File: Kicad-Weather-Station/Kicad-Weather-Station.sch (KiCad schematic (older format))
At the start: 41 parts

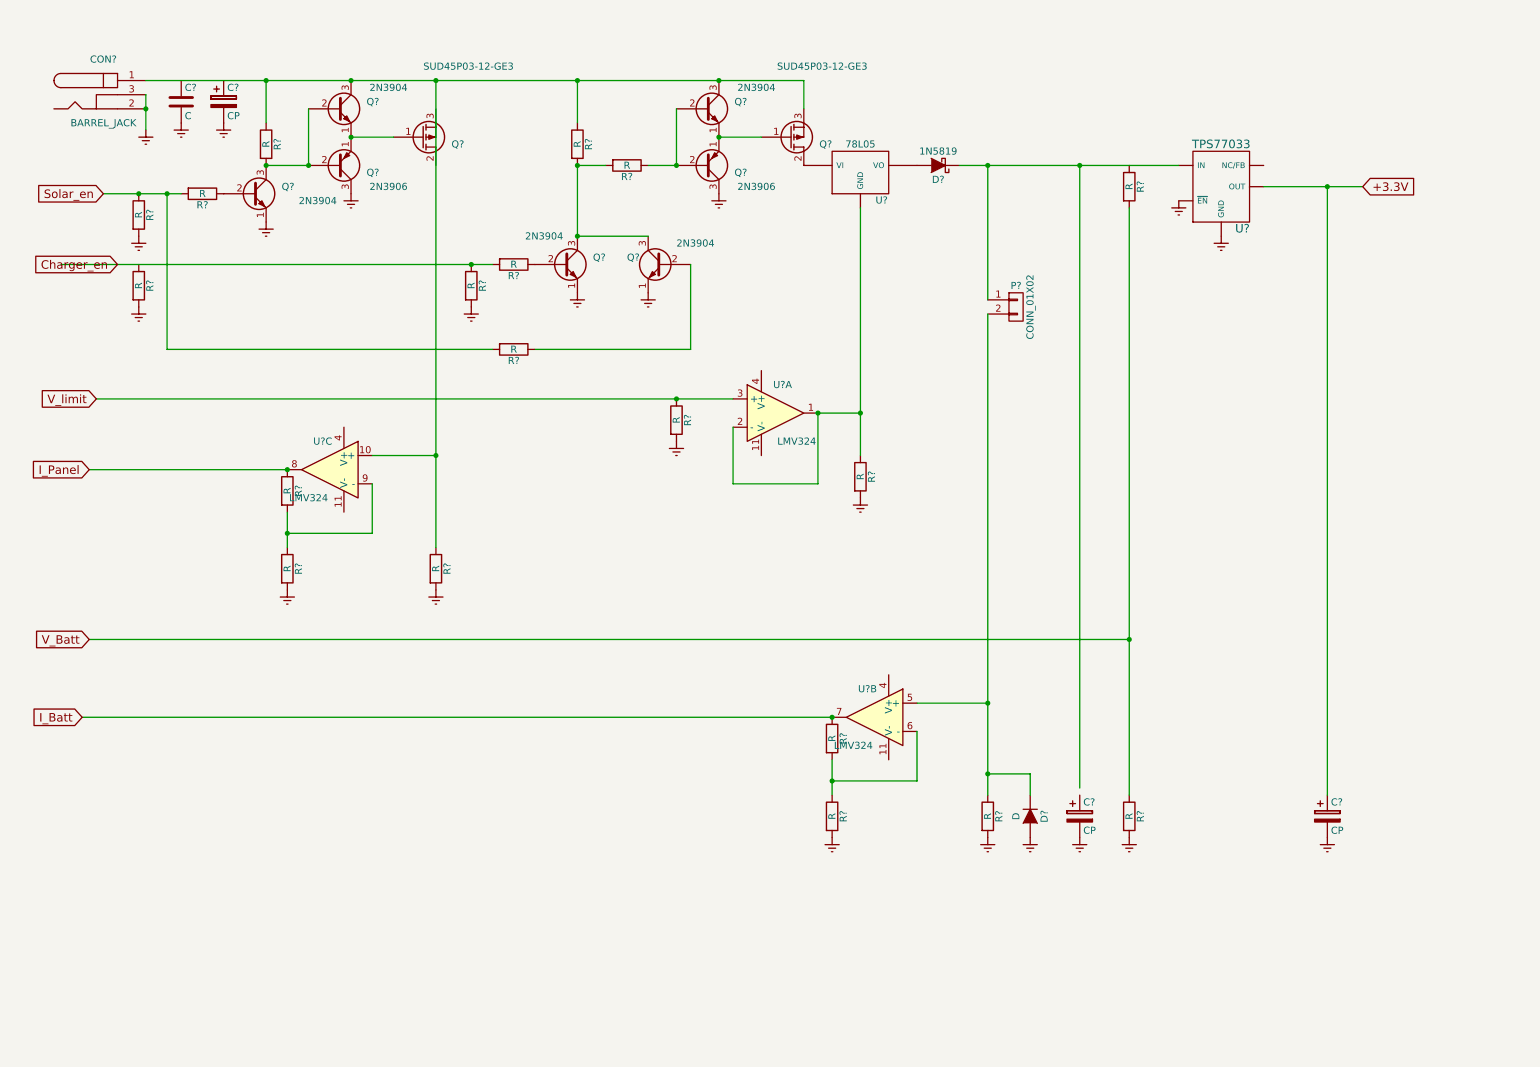
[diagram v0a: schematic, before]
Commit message: Update to schematics. Kicad version completed with values and annotation.
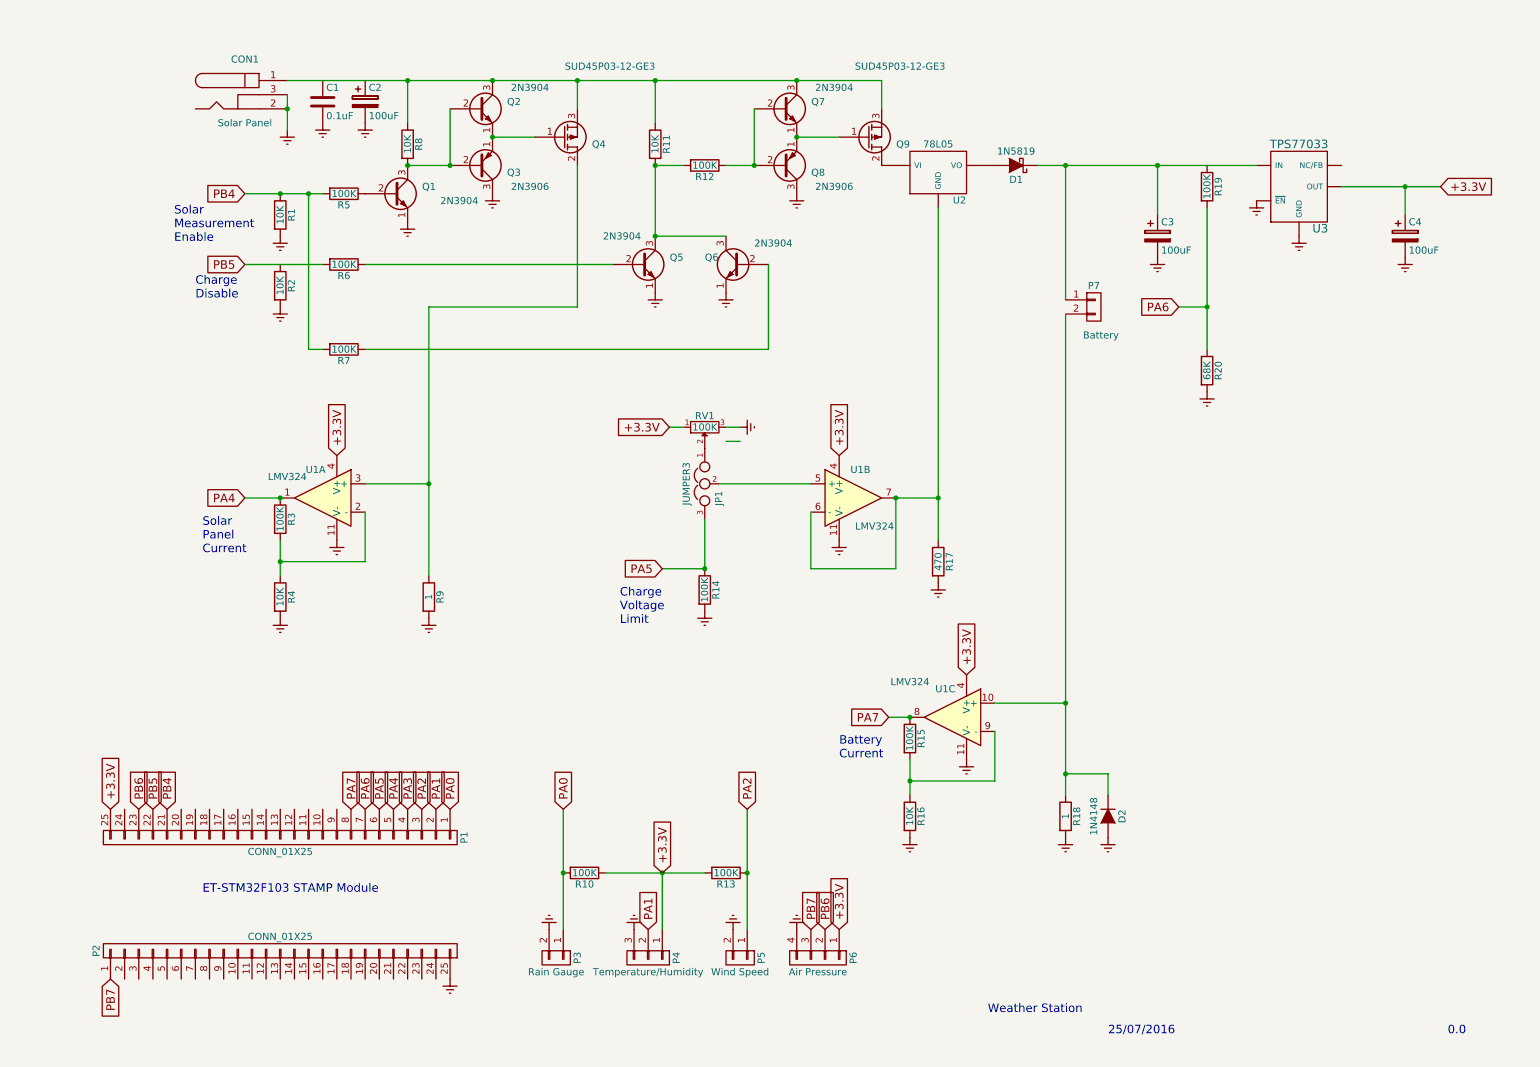
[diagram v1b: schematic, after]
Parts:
- removed R?: R, symbol R
- added JP1: JUMPER3, symbol JUMPER3
- added P1, P2: CONN_01X25, symbol CONN_01X25
- added P3: Rain Gauge, symbol CONN_01X02
- added P4: Temperature/Humidity, symbol CONN_01X03
- added P5: Wind Speed, symbol CONN_01X02
- added P6: Air Pressure, symbol CONN_01X04
- added R10, R13: 100K, symbol R
- added RV1: 100K, symbol POT
- C1: renamed from C?; value C -> 0.1uF
- C2, C3, C4: renamed from C?; value CP -> 100uF
- CON1: renamed from CON?; value BARREL_JACK -> Solar Panel
- D2: renamed from D?; value D -> 1N4148
- P7: renamed from P?; value CONN_01X02 -> Battery
- R1, R11, R16, R2, R4, R8: renamed from R?; value R -> 10K
- R12, R14, R15, R19, R3, R5, R6, R7: renamed from R?; value R -> 100K
- R17: renamed from R?; value R -> 470
- R18, R9: renamed from R?; value R -> 1
- R20: renamed from R?; value R -> 68K
- gave numbers to parts that had none: 13
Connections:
- net labels added: PA0, PA1, PA2, PA3, PA4, PA5, PA6, PA7, PB4, PB5, PB6, PB7
- net labels removed: Charger_en, I_Batt, I_Panel, Solar_en, V_Batt, V_limit
- wire segments 47 -> 81
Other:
- note added: "0.0"
- note added: "25/07/2016"
- note added: "Battery\nCurrent"
- note added: "Charge\nDisable"
- note added: "Charge\nVoltage\nLimit"
- note added: "ET-STM32F103 STAMP Module"
- note added: "Solar\nMeasurement\nEnable"
- note added: "Solar\nPanel\nCurrent"
- note added: "Weather Station"
- moved on the sheet: C1, C2, C3, C4, CON1, D1, D2, P7, Q1, Q2, Q3, Q4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

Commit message: Add footprints and create PCB. Some layout started. Trimpot footprint to be defined.
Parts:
- C1: footprint (none) -> WeatherStation:SM0603_Capa
- C2, C3, C4: footprint (none) -> WeatherStation:SM1206POL
- CON1: footprint (none) -> WeatherStation:BARREL_JACK
- D1: value 1N5819 -> MBR0520LT1G; footprint (none) -> WeatherStation:SOD-123
- D2: footprint (none) -> WeatherStation:SOD-523
- JP1, P4: footprint (none) -> WeatherStation:PINHEAD1-3
- P1, P2: footprint (none) -> WeatherStation:Pin_Header_Straight_1x25
- P3, P5, P7: footprint (none) -> WeatherStation:PINHEAD1-2
- P6: footprint (none) -> WeatherStation:PINHEAD1-4
- Q1, Q2, Q5, Q6, Q7: value 2N3904 -> MMBT3904; footprint (none) -> WeatherStation:SOT23EBC
- Q3, Q8: value 2N3906 -> MMBT3906; footprint (none) -> WeatherStation:SOT23EBC
- Q4, Q9: footprint (none) -> WeatherStation:TO-252-2Lead
- R1, R10, R11, R12, R13, R14, R15, R16, R17, R18, R19, R2, R20, R3, R4, R5, R6, R7, R8, R9: footprint (none) -> WeatherStation:SM0603_Resistor
- RV1: footprint (none) -> Potentiometers:Potentiometer_Bourns_3339P_Angular_ScrewUp
- U1: footprint (none) -> WeatherStation:SOIC-14_N
- U2: value 78L05 -> 78M05; footprint (none) -> WeatherStation:TO-252-2Lead
- U3: footprint (none) -> WeatherStation:SOT23-5
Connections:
- net labels removed: PA3
- wire segments 81 -> 60
- no-connect marks 0 -> 38

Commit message: Oops! forgot the microSD card. Rearrangement of PCB layout to accommodate.
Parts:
- removed U2: 78M05, WeatherStation:TO-252-2Lead, symbol 78L05
- added J1: MicroSD, WeatherStation:Conn_uSDcard, symbol MicroSD
- added R10, R11, R12, R13, R14: 100K, WeatherStation:SM0603_Resistor, symbol R
- added U2: 78M05, WeatherStation:TO-252-2Lead, symbol 78M05
- C4: value 100uF -> 10uF
- renumbered R10 to R15, R11 to R16, R12 to R17, R14 to R18, R13 to R19, R15 to R20, R16 to R21, R17 to R22, R18 to R23, R19 to R24, R20 to R25
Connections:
- net labels added: PB12, PB13, PB14, PB15, RSRVD
- wire segments 60 -> 61
- no-connect marks 38 -> 35
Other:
- moved on the sheet: P1, P2

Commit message: First form of PCB
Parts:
- added P10, P11, P12, P8, P9: CONN_01X01, WeatherStation:SIL-1, symbol CONN_01X01
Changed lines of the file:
@@
 Connection ~ 3850 7300
 NoConn ~ 1350 7000
+$Comp
+L CONN_01X01 P8
+U 1 1 5798030E
+P 8950 3800
+F 0 "P8" H 8950 3900 50  0000 C CNN
+F 1 "CONN_01X01" V 9050 3800 50  0000 C CNN
+F 2 "WeatherStation:SIL-1" H 8950 3800 50  0001 C CNN
+F 3 "" H 8950 3800 50  0000 C CNN
+	1    8950 3800
+	1    0    0    -1
+$EndComp
+$Comp
+L CONN_01X01 P9
+U 1 1 579803AD
+P 8950 4050
+F 0 "P9" H 8950 4150 50  0000 C CNN
+F 1 "CONN_01X01" V 9050 4050 50  0000 C CNN
+F 2 "WeatherStation:SIL-1" H 8950 4050 50  0001 C CNN
+F 3 "" H 8950 4050 50  0000 C CNN
+	1    8950 4050
+	1    0    0    -1
+$EndComp
+$Comp
+L CONN_01X01 P10
+U 1 1 57980464
+P 8950 4300
+F 0 "P10" H 8950 4400 50  0000 C CNN
+F 1 "CONN_01X01" V 9050 4300 50  0000 C CNN
+F 2 "WeatherStation:SIL-1" H 8950 4300 50  0001 C CNN
+F 3 "" H 8950 4300 50  0000 C CNN
+	1    8950 4300
+	1    0    0    -1
+$EndComp
+$Comp
+L CONN_01X01 P11
+U 1 1 57980521
+P 8950 4600
+F 0 "P11" H 8950 4700 50  0000 C CNN
+F 1 "CONN_01X01" V 9050 4600 50  0000 C CNN
+F 2 "WeatherStation:SIL-1" H 8950 4600 50  0001 C CNN
+F 3 "" H 8950 4600 50  0000 C CNN
+	1    8950 4600
+	1    0    0    -1
+$EndComp
+$Comp
+L Earth #PWR?
+U 1 1 5798550B
+P 8750 3800
+F 0 "#PWR?" H 8750 3550 50  0001 C CNN
+F 1 "Earth" H 8750 3650 50  0001 C CNN
+F 2 "" H 8750 3800 50  0000 C CNN
+F 3 "" H 8750 3800 50  0000 C CNN
+	1    8750 3800
+	1    0    0    -1
+$EndComp
+$Comp
+L Earth #PWR?
+U 1 1 579855CA
+P 8750 4050
+F 0 "#PWR?" H 8750 3800 50  0001 C CNN
+F 1 "Earth" H 8750 3900 50  0001 C CNN
+F 2 "" H 8750 4050 50  0000 C CNN
+F 3 "" H 8750 4050 50  0000 C CNN
+	1    8750 4050
+	1    0    0    -1
+$EndComp
+$Comp
+L Earth #PWR?
+U 1 1 57985689
+P 8750 4300
+F 0 "#PWR?" H 8750 4050 50  0001 C CNN
+F 1 "Earth" H 8750 4150 50  0001 C CNN
+F 2 "" H 8750 4300 50  0000 C CNN
+F 3 "" H 8750 4300 50  0000 C CNN
+	1    8750 4300
+	1    0    0    -1
+$EndComp
+$Comp
+L Earth #PWR?
+U 1 1 57985748
+P 8750 4600
+F 0 "#PWR?" H 8750 4350 50  0001 C CNN
+F 1 "Earth" H 8750 4450 50  0001 C CNN
+F 2 "" H 8750 4600 50  0000 C CNN
+F 3 "" H 8750 4600 50  0000 C CNN
+	1    8750 4600
+	1    0    0    -1
+$EndComp
+$Comp
+L CONN_01X01 P12
+U 1 1 57986893
+P 8950 4900
+F 0 "P12" H 8950 5000 50  0000 C CNN
+F 1 "CONN_01X01" V 9050 4900 50  0000 C CNN
+F 2 "WeatherStation:SIL-1" H 8950 4900 50  0001 C CNN
+F 3 "" H 8950 4900 50  0000 C CNN
+	1    8950 4900
+	1    0    0    -1
+$EndComp
+$Comp
+L Earth #PWR?
+U 1 1 57986899
+P 8750 4600
+F 0 "#PWR?" H 8750 4350 50  0001 C CNN
+F 1 "Earth" H 8750 4450 50  0001 C CNN
+F 2 "" H 8750 4600 50  0000 C CNN
+F 3 "" H 8750 4600 50  0000 C CNN
+	1    8750 4600
+	1    0    0    -1
+$EndComp
+$Comp
+L Earth #PWR?
+U 1 1 5798689F
+P 8750 4900
+F 0 "#PWR?" H 8750 4650 50  0001 C CNN
+F 1 "Earth" H 8750 4750 50  0001 C CNN
+F 2 "" H 8750 4900 50  0000 C CNN
+F 3 "" H 8750 4900 50  0000 C CNN
+	1    8750 4900
+	1    0    0    -1
+$EndComp
 $EndSCHEMATC

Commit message: Add Amphenol microSD connector to PCB.
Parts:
- J1: footprint WeatherStation:Conn_uSDcard -> WeatherStation:Conn_uSDcard_Amph_114_00841_68
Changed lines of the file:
@@
 F 0 "J1" H 1750 7900 60  0000 C CNN
 F 1 "MicroSD" H 1750 6500 60  0000 C CNN
-F 2 "WeatherStation:Conn_uSDcard" H 2050 7350 60  0001 C CNN
+F 2 "WeatherStation:Conn_uSDcard_Amph_114_00841_68" H 2050 7350 60  0001 C CNN
 F 3 "" H 2050 7350 60  0000 C CNN
 	1    1950 7200
@@
 $EndComp
 $Comp
-L Earth #PWR?
+L Earth #PWR038
 U 1 1 5798550B
 P 8750 3800
-F 0 "#PWR?" H 8750 3550 50  0001 C CNN
+F 0 "#PWR038" H 8750 3550 50  0001 C CNN
 F 1 "Earth" H 8750 3650 50  0001 C CNN
 F 2 "" H 8750 3800 50  0000 C CNN
@@
 $EndComp
 $Comp
-L Earth #PWR?
+L Earth #PWR039
 U 1 1 579855CA
 P 8750 4050
-F 0 "#PWR?" H 8750 3800 50  0001 C CNN
+F 0 "#PWR039" H 8750 3800 50  0001 C CNN
 F 1 "Earth" H 8750 3900 50  0001 C CNN
 F 2 "" H 8750 4050 50  0000 C CNN
@@
 $EndComp
 $Comp
-L Earth #PWR?
+L Earth #PWR040
 U 1 1 57985689
 P 8750 4300
-F 0 "#PWR?" H 8750 4050 50  0001 C CNN
+F 0 "#PWR040" H 8750 4050 50  0001 C CNN
 F 1 "Earth" H 8750 4150 50  0001 C CNN
 F 2 "" H 8750 4300 50  0000 C CNN
@@
 $EndComp
 $Comp
-L Earth #PWR?
+L Earth #PWR041
 U 1 1 57985748
 P 8750 4600
-F 0 "#PWR?" H 8750 4350 50  0001 C CNN
+F 0 "#PWR041" H 8750 4350 50  0001 C CNN
 F 1 "Earth" H 8750 4450 50  0001 C CNN
 F 2 "" H 8750 4600 50  0000 C CNN
@@
 $EndComp
 $Comp
-L Earth #PWR?
+L Earth #PWR042
 U 1 1 57986899
 P 8750 4600
-F 0 "#PWR?" H 8750 4350 50  0001 C CNN
+F 0 "#PWR042" H 8750 4350 50  0001 C CNN
 F 1 "Earth" H 8750 4450 50  0001 C CNN
 F 2 "" H 8750 4600 50  0000 C CNN
@@
 $EndComp
 $Comp
-L Earth #PWR?
+L Earth #PWR043
 U 1 1 5798689F
 P 8750 4900
-F 0 "#PWR?" H 8750 4650 50  0001 C CNN
+F 0 "#PWR043" H 8750 4650 50  0001 C CNN
 F 1 "Earth" H 8750 4750 50  0001 C CNN
 F 2 "" H 8750 4900 50  0000 C CNN

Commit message: Add Amphenol microSD connector to PCB and add the CP (card present) signal to PA8.
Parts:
- added R26: 100K, WeatherStation:SM0603_Resistor, symbol R
- J1: symbol MicroSD -> MicroSD_Amph_114_00841_68
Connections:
- net labels added: PA8
- no-connect marks 35 -> 34
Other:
- moved on the sheet: R10, R11, R12, R13, R14
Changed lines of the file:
@@
 NoConn ~ 1550 6100
 NoConn ~ 1450 6100
-NoConn ~ 2900 5150
 NoConn ~ 2800 5150
 NoConn ~ 2700 5150
@@
 $EndComp
 $Comp
-L MicroSD J1
+L MicroSD_Amph_114_00841_68 J1
 U 1 1 5798C59E
 P 1950 7200
 F 0 "J1" H 1750 7900 60  0000 C CNN
-F 1 "MicroSD" H 1750 6500 60  0000 C CNN
+F 1 "MicroSD" H 1750 6250 60  0000 C CNN
 F 2 "WeatherStation:Conn_uSDcard_Amph_114_00841_68" H 2050 7350 60  0001 C CNN
 F 3 "" H 2050 7350 60  0000 C CNN
@@
 Text GLabel 1550 7000 1    60   Input ~ 0
 PB15
-Text GLabel 3850 6700 1    60   Input ~ 0
+Text GLabel 4050 6500 1    60   Input ~ 0
 +3.3V
-Text GLabel 3550 6850 0    60   Input ~ 0
+Text GLabel 3750 6850 0    60   Input ~ 0
 PB12
-Text GLabel 3550 7000 0    60   Input ~ 0
+Text GLabel 3750 7000 0    60   Input ~ 0
 PB13
-Text GLabel 3550 7150 0    60   Input ~ 0
+Text GLabel 3750 7150 0    60   Input ~ 0
 PB14
-Text GLabel 3550 7300 0    60   Input ~ 0
+Text GLabel 3750 7300 0    60   Input ~ 0
 PB15
 Text GLabel 1650 7000 1    60   Input ~ 0
@@
 Text GLabel 2050 7000 1    60   Input ~ 0
 RSRVD
-Text GLabel 3550 7450 0    60   Input ~ 0
+Text GLabel 3750 7450 0    60   Input ~ 0
 RSRVD
 $Comp
@@
 L R R10
 U 1 1 579728DF
-P 3700 6850
-F 0 "R10" V 3780 6850 50  0000 C CNN
-F 1 "100K" V 3700 6850 50  0000 C CNN
-F 2 "WeatherStation:SM0603_Resistor" V 3630 6850 50  0001 C CNN
-F 3 "" H 3700 6850 50  0000 C CNN
-	1    3700 6850
+P 3900 6850
+F 0 "R10" V 3980 6850 50  0000 C CNN
+F 1 "100K" V 3900 6850 50  0000 C CNN
+F 2 "WeatherStation:SM0603_Resistor" V 3830 6850 50  0001 C CNN
+F 3 "" H 3900 6850 50  0000 C CNN
+	1    3900 6850
 	0    1    1    0
 $EndComp
@@
 L R R11
 U 1 1 57972AB3
-P 3700 7000
-F 0 "R11" V 3780 7000 50  0000 C CNN
-F 1 "100K" V 3700 7000 50  0000 C CNN
-F 2 "WeatherStation:SM0603_Resistor" V 3630 7000 50  0001 C CNN
-F 3 "" H 3700 7000 50  0000 C CNN
-	1    3700 7000
+P 3900 7000
+F 0 "R11" V 3980 7000 50  0000 C CNN
+F 1 "100K" V 3900 7000 50  0000 C CNN
+F 2 "WeatherStation:SM0603_Resistor" V 3830 7000 50  0001 C CNN
+F 3 "" H 3900 7000 50  0000 C CNN
+	1    3900 7000
 	0    1    1    0
 $EndComp
@@
 L R R12
 U 1 1 57972B68
-P 3700 7150
-F 0 "R12" V 3780 7150 50  0000 C CNN
-F 1 "100K" V 3700 7150 50  0000 C CNN
-F 2 "WeatherStation:SM0603_Resistor" V 3630 7150 50  0001 C CNN
-F 3 "" H 3700 7150 50  0000 C CNN
-	1    3700 7150
+P 3900 7150
+F 0 "R12" V 3980 7150 50  0000 C CNN
+F 1 "100K" V 3900 7150 50  0000 C CNN
+F 2 "WeatherStation:SM0603_Resistor" V 3830 7150 50  0001 C CNN
+F 3 "" H 3900 7150 50  0000 C CNN
+	1    3900 7150
 	0    1    1    0
 $EndComp
@@
 L R R13
 U 1 1 57972C20
-P 3700 7300
-F 0 "R13" V 3780 7300 50  0000 C CNN
-F 1 "100K" V 3700 7300 50  0000 C CNN
-F 2 "WeatherStation:SM0603_Resistor" V 3630 7300 50  0001 C CNN
-F 3 "" H 3700 7300 50  0000 C CNN
-	1    3700 7300
+P 3900 7300
+F 0 "R13" V 3980 7300 50  0000 C CNN
+F 1 "100K" V 3900 7300 50  0000 C CNN
+F 2 "WeatherStation:SM0603_Resistor" V 3830 7300 50  0001 C CNN
+F 3 "" H 3900 7300 50  0000 C CNN
+	1    3900 7300
 	0    1    1    0
 $EndComp
@@
 L R R14
 U 1 1 57972CDF
-P 3700 7450
-F 0 "R14" V 3780 7450 50  0000 C CNN
-F 1 "100K" V 3700 7450 50  0000 C CNN
-F 2 "WeatherStation:SM0603_Resistor" V 3630 7450 50  0001 C CNN
-F 3 "" H 3700 7450 50  0000 C CNN
-	1    3700 7450
+P 3900 7450
+F 0 "R14" V 3980 7450 50  0000 C CNN
+F 1 "100K" V 3900 7450 50  0000 C CNN
+F 2 "WeatherStation:SM0603_Resistor" V 3830 7450 50  0001 C CNN
+F 3 "" H 3900 7450 50  0000 C CNN
+	1    3900 7450
 	0    1    1    0
 $EndComp
@@
 Connection ~ 3400 900
 Wire Wire Line
-	3400 1200 3400 900
+	3400 900  3400 1200
 Wire Wire Line
 	2550 900  6750 900
@@
 Connection ~ 9050 1500
 Wire Wire Line
-	3100 1200 2550 1200
+	2550 1200 3100 1200
 Connection ~ 2550 1200
 Connection ~ 2800 1200
 Connection ~ 9400 1500
 Wire Wire Line
-	3850 6700 3850 7450
-Connection ~ 3850 6850
-Connection ~ 3850 7000
-Connection ~ 3850 7150
-Connection ~ 3850 7300
+	4050 6500 4050 7450
+Connection ~ 4050 6850
+Connection ~ 4050 7000
+Connection ~ 4050 7150
+Connection ~ 4050 7300
 NoConn ~ 1350 7000
 $Comp
@@
 	1    0    0    -1
 $EndComp
+$Comp
+L Earth #PWR044
+U 1 1 57C198FD
+P 2750 7000
+F 0 "#PWR044" H 2750 6750 50  0001 C CNN
+F 1 "Earth" H 2750 6850 50  0001 C CNN
+F 2 "" H 2750 7000 50  0000 C CNN
+F 3 "" H 2750 7000 50  0000 C CNN
+	1    2750 7000
+	-1   0    0    1
+$EndComp
+$Comp
+L R R26
+U 1 1 57C19F76
+P 3900 6700
+F 0 "R26" V 3980 6700 50  0000 C CNN
+F 1 "100K" V 3900 6700 50  0000 C CNN
+F 2 "WeatherStation:SM0603_Resistor" V 3830 6700 50  0001 C CNN
+F 3 "" H 3900 6700 50  0000 C CNN
+	1    3900 6700
+	0    1    1    0
+$EndComp
+Text GLabel 2900 5150 1    60   Input ~ 0
+PA8
+Text GLabel 3750 6700 0    60   Input ~ 0
+PA8
+Text GLabel 2650 7000 1    60   Input ~ 0
+PA8
+Connection ~ 4050 6700
 $EndSCHEMATC

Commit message: Add a sensor enable circuit to allow switching of power to sensors that are used only when the processor is awake, to save energy.
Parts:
- added Q10, Q11: MMBT3904, WeatherStation:SOT23EBC, symbol Q_NPN_EBC
- added Q12: MMBT3906, WeatherStation:SOT23EBC, symbol Q_PNP_EBC
- added Q13: SUD45P03-12-GE3, WeatherStation:TO-252-2Lead, symbol Q_PMOS_GDS
- added R? (x2): 10K, WeatherStation:SM0603_Resistor, symbol R
- added R?: 100K, WeatherStation:SM0603_Resistor, symbol R
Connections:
- net labels added: PB3, PD2
- net labels removed: PA8
- wire segments 61 -> 72
- no-connect marks 34 -> 32
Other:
- note added: "Sensor Power\nEnable"
- moved on the sheet: JP1, P4, P5, Q6, R18, R19, R20, R21, R22, R3, R4, R7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
